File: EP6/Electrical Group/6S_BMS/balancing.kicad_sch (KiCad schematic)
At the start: 16 parts

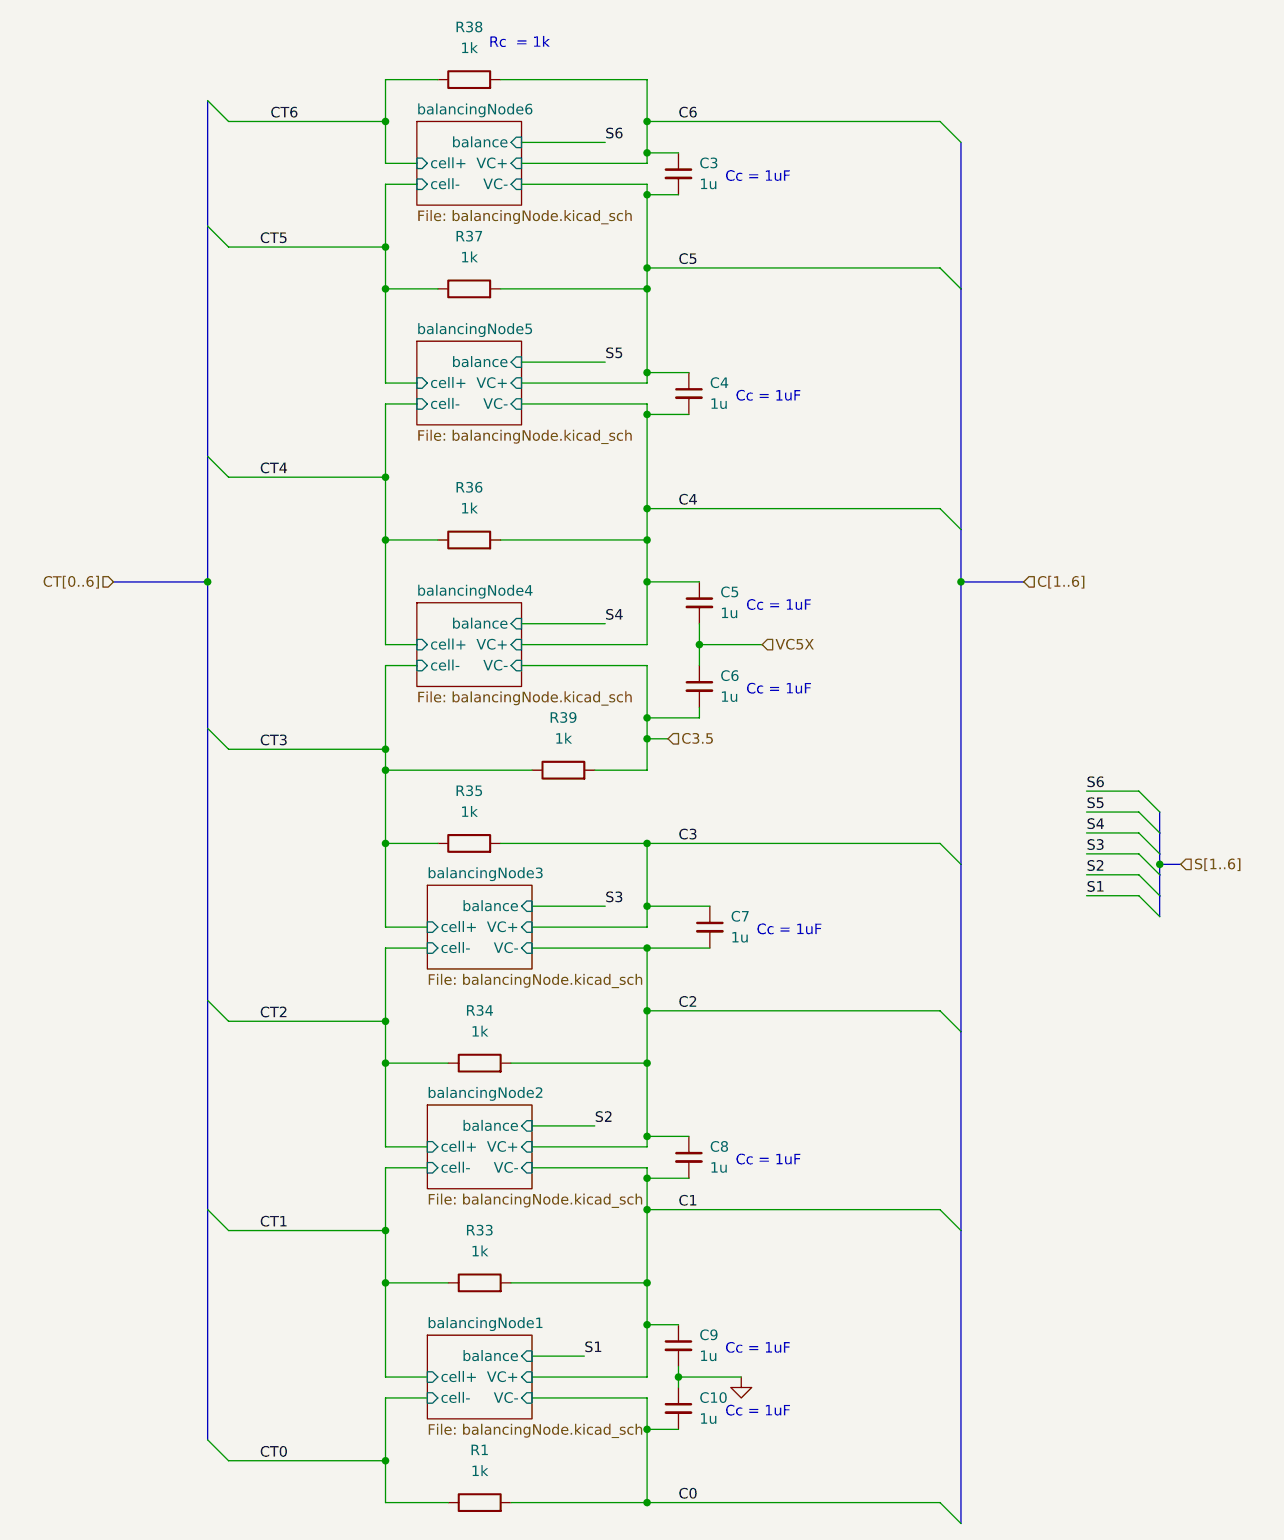
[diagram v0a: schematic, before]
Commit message: update 6S_BMS schematic, for FET and Balancing
use highside FET for charge and discharge switch
and use chip for balance rather than MCU
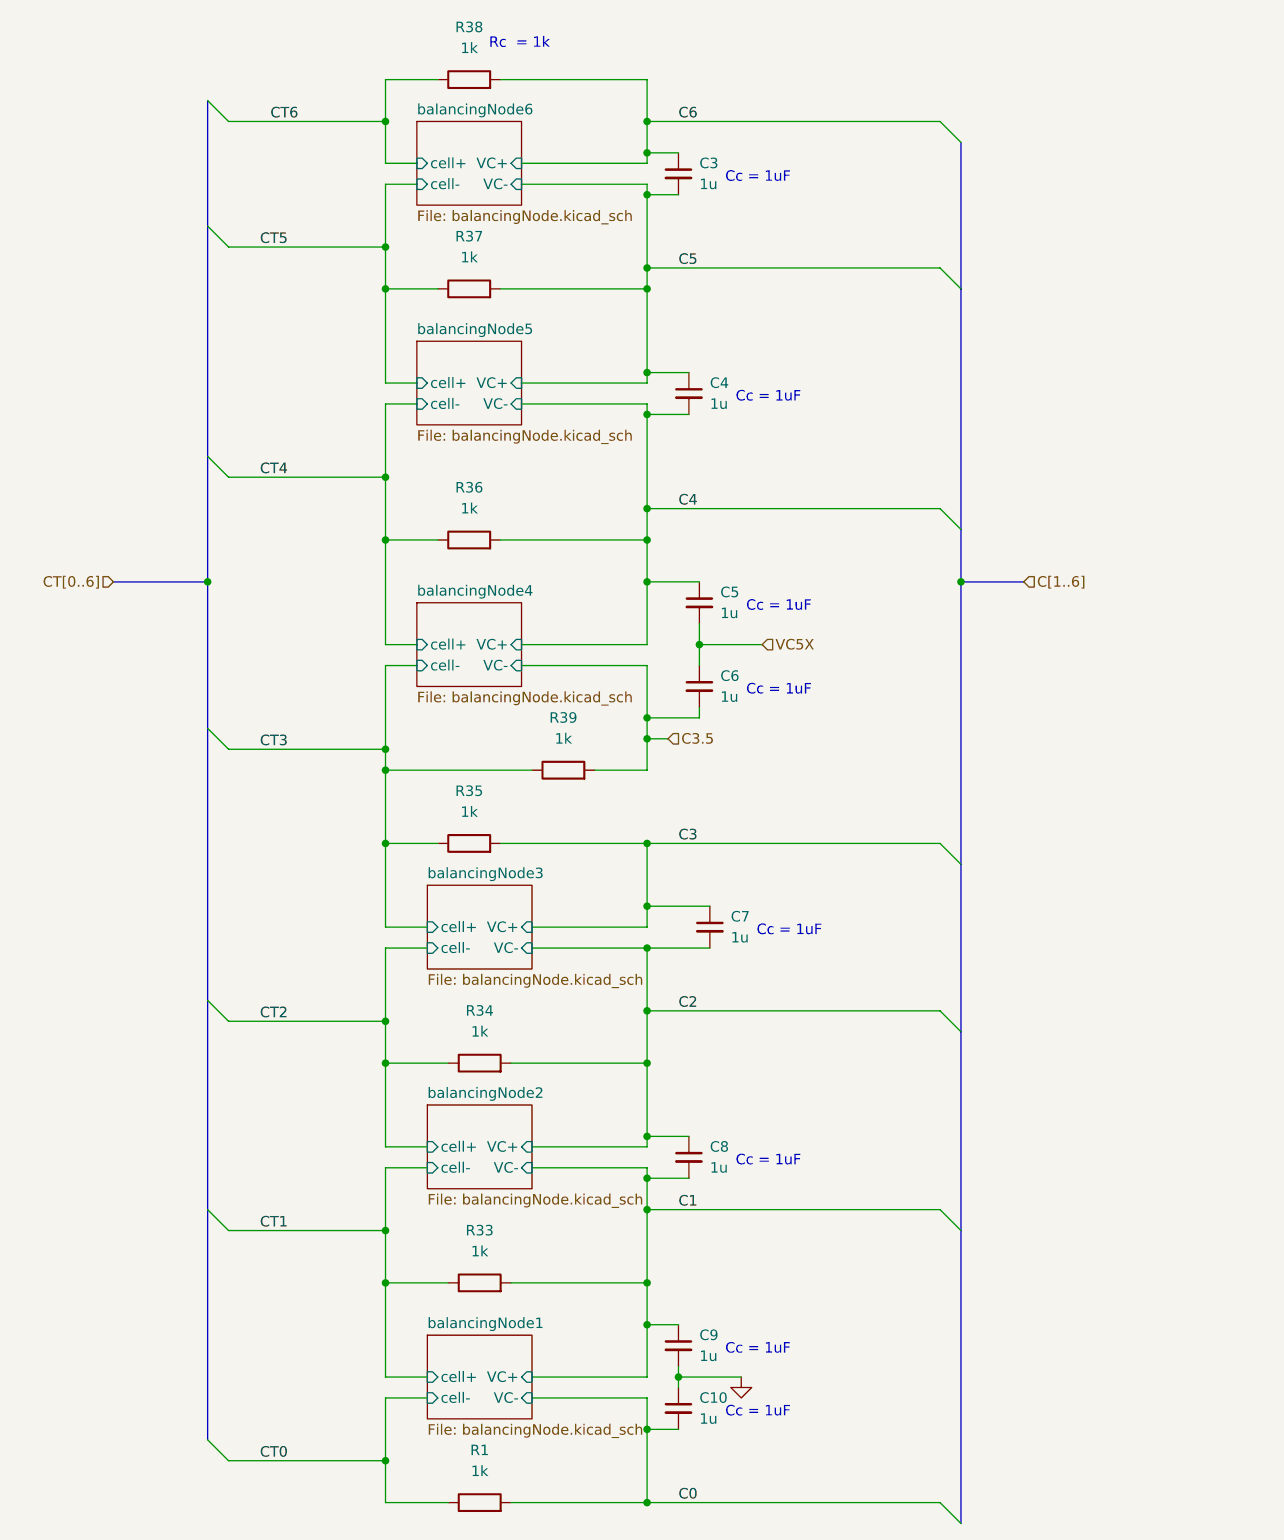
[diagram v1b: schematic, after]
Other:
- sheet balancingNode1 ports: added none; removed balance
- sheet balancingNode2 ports: added none; removed balance
- sheet balancingNode3 ports: added none; removed balance
- sheet balancingNode4 ports: added none; removed balance
- sheet balancingNode5 ports: added none; removed balance
- sheet balancingNode6 ports: added none; removed balance

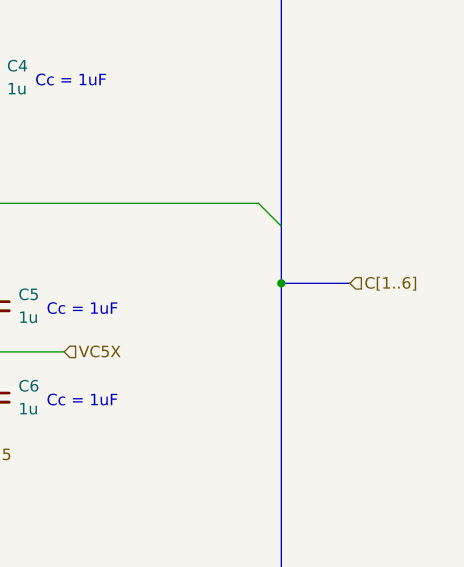
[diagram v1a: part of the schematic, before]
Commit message: update 6S_BMS  schematic and a little layout
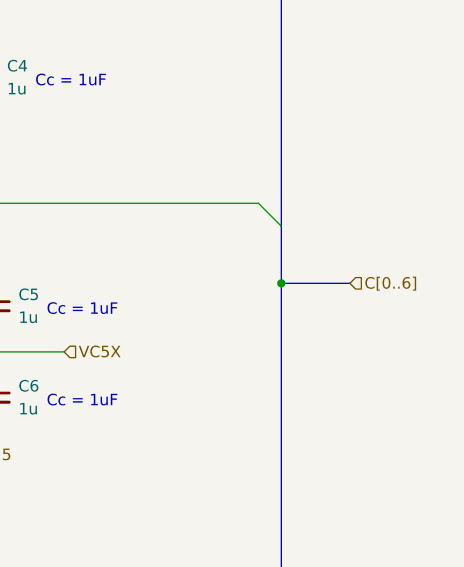
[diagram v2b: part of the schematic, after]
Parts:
- C10, C3, C4, C5, C6, C7, C8, C9: footprint Capacitor_SMD:C_0603_1608Metric -> Capacitor_SMD:C_0402_1005Metric
- R1, R33, R34, R35, R36, R37, R38, R39: footprint Resistor_SMD:R_0603_1608Metric -> Resistor_SMD:R_0402_1005Metric
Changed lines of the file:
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@@
 		)
 	)
-	(hierarchical_label "C[1..6]"
+	(hierarchical_label "C[0..6]"
 		(shape input)
 		(at 167.64 81.28 0)
@@
 			)
 		)
-		(property "Footprint" "Resistor_SMD:R_0603_1608Metric"
+		(property "Footprint" "Resistor_SMD:R_0402_1005Metric"
 			(at 111.76 105.918 90)
 			(effects
@@
 			)
 		)
-		(property "Description" ""
+		(property "Description" "Resistor"
 			(at 111.76 104.14 0)
 			(effects
@@
 			)
 		)
-		(property "Footprint" "Capacitor_SMD:C_0603_1608Metric"
+		(property "Footprint" "Capacitor_SMD:C_0402_1005Metric"
 			(at 128.27 83.82 0)
 			(effects
@@
 			)
 		)
-		(property "Footprint" "Resistor_SMD:R_0603_1608Metric"
+		(property "Footprint" "Resistor_SMD:R_0402_1005Metric"
 			(at 101.6 194.818 90)
 			(effects
@@
 			)
 		)
-		(property "Description" ""
+		(property "Description" "Resistor"
 			(at 101.6 193.04 0)
 			(effects
@@
 	)
 	(symbol
-		(lib_name "GND_1")
 		(lib_id "power:GND")
 		(at 133.35 177.8 0)
@@
 			)
 		)
-		(property "Footprint" "Capacitor_SMD:C_0603_1608Metric"
+		(property "Footprint" "Capacitor_SMD:C_0402_1005Metric"
 			(at 125.73 181.61 0)
 			(effects
@@
 			)
 		)
-		(property "Footprint" "Resistor_SMD:R_0603_1608Metric"
+		(property "Footprint" "Resistor_SMD:R_0402_1005Metric"
 			(at 101.6 141.478 90)
 			(effects
@@
 			)
 		)
-		(property "Description" ""
+		(property "Description" "Resistor"
 			(at 101.6 139.7 0)
 			(effects
@@
 			)
 		)
-		(property "Footprint" "Resistor_SMD:R_0603_1608Metric"
+		(property "Footprint" "Resistor_SMD:R_0402_1005Metric"
 			(at 101.6 168.148 90)
 			(effects
@@
 			)
 		)
-		(property "Description" ""
+		(property "Description" "Resistor"
 			(at 101.6 166.37 0)
 			(effects
@@
 			)
 		)
-		(property "Footprint" "Capacitor_SMD:C_0603_1608Metric"
+		(property "Footprint" "Capacitor_SMD:C_0402_1005Metric"
 			(at 127 58.42 0)
 			(effects
@@
 			)
 		)
-		(property "Footprint" "Capacitor_SMD:C_0603_1608Metric"
+		(property "Footprint" "Capacitor_SMD:C_0402_1005Metric"
 			(at 127 151.13 0)
 			(effects
@@
 			)
 		)
-		(property "Footprint" "Capacitor_SMD:C_0603_1608Metric"
+		(property "Footprint" "Capacitor_SMD:C_0402_1005Metric"
 			(at 128.27 93.98 0)
 			(effects
@@
 			)
 		)
-		(property "Footprint" "Capacitor_SMD:C_0603_1608Metric"
+		(property "Footprint" "Capacitor_SMD:C_0402_1005Metric"
 			(at 125.73 31.75 0)
 			(effects
@@
 			)
 		)
-		(property "Footprint" "Resistor_SMD:R_0603_1608Metric"
+		(property "Footprint" "Resistor_SMD:R_0402_1005Metric"
 			(at 100.33 77.978 90)
 			(effects
@@
 			)
 		)
-		(property "Description" ""
+		(property "Description" "Resistor"
 			(at 100.33 76.2 0)
 			(effects
@@
 			)
 		)
-		(property "Footprint" "Capacitor_SMD:C_0603_1608Metric"
+		(property "Footprint" "Capacitor_SMD:C_0402_1005Metric"
 			(at 125.73 173.99 0)
 			(effects
@@
 			)
 		)
-		(property "Footprint" "Resistor_SMD:R_0603_1608Metric"
+		(property "Footprint" "Resistor_SMD:R_0402_1005Metric"
 			(at 100.33 47.498 90)
 			(effects
@@
 			)
 		)
-		(property "Description" ""
+		(property "Description" "Resistor"
 			(at 100.33 45.72 0)
 			(effects
@@
 			)
 		)
-		(property "Footprint" "Capacitor_SMD:C_0603_1608Metric"
+		(property "Footprint" "Capacitor_SMD:C_0402_1005Metric"
 			(at 129.54 123.19 0)
 			(effects
@@
 			)
 		)
-		(property "Footprint" "Resistor_SMD:R_0603_1608Metric"
+		(property "Footprint" "Resistor_SMD:R_0402_1005Metric"
 			(at 100.33 114.808 90)
 			(effects
@@
 			)
 		)
-		(property "Description" ""
+		(property "Description" "Resistor"
 			(at 100.33 113.03 0)
 			(effects
@@
 			)
 		)
-		(property "Footprint" "Resistor_SMD:R_0603_1608Metric"
+		(property "Footprint" "Resistor_SMD:R_0402_1005Metric"
 			(at 100.33 22.098 90)
 			(effects
@@
 			)
 		)
-		(property "Description" ""
+		(property "Description" "Resistor"
 			(at 100.33 20.32 0)
 			(effects
@@
 			(project "6S_BMS"
 				(path "/0942010f-46b1-4fe9-9f5e-a3ebd22b3e41/83cfee2e-408d-40a7-bf01-d9ac25e22570"
-					(page "6")
+					(page "23")
 				)
 			)
@@
 			(project "6S_BMS"
 				(path "/0942010f-46b1-4fe9-9f5e-a3ebd22b3e41/83cfee2e-408d-40a7-bf01-d9ac25e22570"
-					(page "8")
+					(page "25")
 				)
 			)
@@
 			(project "6S_BMS"
 				(path "/0942010f-46b1-4fe9-9f5e-a3ebd22b3e41/83cfee2e-408d-40a7-bf01-d9ac25e22570"
-					(page "4")
+					(page "21")
 				)
 			)
@@
 			(project "6S_BMS"
 				(path "/0942010f-46b1-4fe9-9f5e-a3ebd22b3e41/83cfee2e-408d-40a7-bf01-d9ac25e22570"
-					(page "5")
+					(page "22")
 				)
 			)
@@
 			(project "6S_BMS"
 				(path "/0942010f-46b1-4fe9-9f5e-a3ebd22b3e41/83cfee2e-408d-40a7-bf01-d9ac25e22570"
-					(page "7")
+					(page "24")
 				)
 			)
@@
 			(project "6S_BMS"
 				(path "/0942010f-46b1-4fe9-9f5e-a3ebd22b3e41/83cfee2e-408d-40a7-bf01-d9ac25e22570"
-					(page "9")
-				)
-			)
+					(page "26")
+				)
+			)
